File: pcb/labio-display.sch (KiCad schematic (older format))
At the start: 0 parts

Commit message: add schematics for display and dio (dpad, servo, motor, encoder)
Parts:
- added P?: CONN_01X12, symbol CONN_01X12
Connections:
- new net GND: P?.1 (P1), P?.12 (P12), P?.8 (P8)
- new net OLED_MOSI: P?.3 (P3)
- new net OLED_SCK: P?.4 (P4)
- new net VDD_3V3: P?.10 (P10), P?.11 (P11), P?.9 (P9)
- new net ~OLED_CS: P?.7 (P7)
- new net ~OLED_RST: P?.6 (P6)
- no-connect marks 0 -> 2
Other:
- note added: "CFAL12832D-B* OLED Display\n3-wire SPI mode."
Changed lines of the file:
@@
 $Descr A4 11693 8268
 encoding utf-8
-Sheet 1 7
+Sheet 5 8
 Title ""
 Date ""
@@
 Comment4 ""
 $EndDescr
+$Comp
+L CONN_01X12 P?
+U 1 1 575D4CD5
+P 5700 2950
+F 0 "P?" H 5700 3600 50  0000 C CNN
+F 1 "CONN_01X12" V 5800 2950 50  0000 C CNN
+F 2 "" H 5700 2950 50  0000 C CNN
+F 3 "" H 5700 2950 50  0000 C CNN
+	1    5700 2950
+	1    0    0    -1
+$EndComp
+Text Notes 4500 2100 0    60   ~ 0
+CFAL12832D-B* OLED Display\n3-wire SPI mode.
+$Comp
+L GND #PWR?
+U 1 1 575D4D1A
+P 4500 3600
+F 0 "#PWR?" H 4500 3350 50  0001 C CNN
+F 1 "GND" H 4500 3450 50  0000 C CNN
+F 2 "" H 4500 3600 50  0000 C CNN
+F 3 "" H 4500 3600 50  0000 C CNN
+	1    4500 3600
+	1    0    0    -1
+$EndComp
+Wire Wire Line
+	4500 2400 4500 3600
+Wire Wire Line
+	4500 3500 5500 3500
+Wire Wire Line
+	4500 2400 5500 2400
+Connection ~ 4500 3500
+Text HLabel 5000 3300 0    60   Input ~ 0
+VDD_3V3
+Wire Wire Line
+	5000 3300 5500 3300
+Wire Wire Line
+	5100 3300 5100 3400
+Wire Wire Line
+	5100 3400 5500 3400
+Connection ~ 5100 3300
+Wire Wire Line
+	5500 3200 5200 3200
+Wire Wire Line
+	5200 3200 5200 3300
+Connection ~ 5200 3300
+Wire Wire Line
+	5500 3100 4500 3100
+Connection ~ 4500 3100
+Text HLabel 5300 3000 0    60   Input ~ 0
+~OLED_CS
+Text HLabel 5300 2900 0    60   Input ~ 0
+~OLED_RST
+NoConn ~ 5500 2800
+Text HLabel 5300 2700 0    60   Input ~ 0
+OLED_SCK
+Text HLabel 5300 2600 0    60   Input ~ 0
+OLED_MOSI
+NoConn ~ 5500 2500
+Wire Wire Line
+	5300 2600 5500 2600
+Wire Wire Line
+	5300 2700 5500 2700
+Wire Wire Line
+	5300 2900 5500 2900
+Wire Wire Line
+	5300 3000 5500 3000
 $EndSCHEMATC

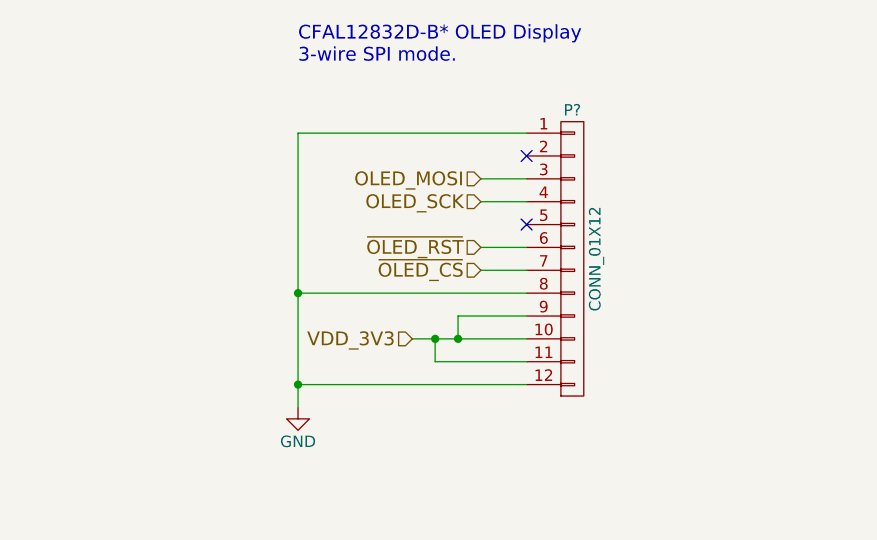
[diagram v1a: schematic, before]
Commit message: add imu sensors, make top level connections
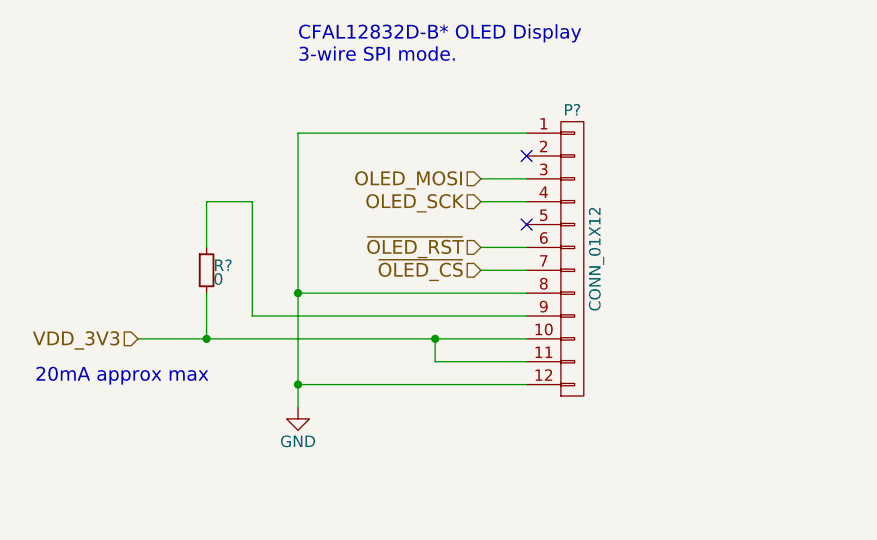
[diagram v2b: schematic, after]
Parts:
- added R?: 0, symbol R_Small
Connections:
- net VDD_3V3: now also R?.2; no longer P?.9 (P9)
- new net: P?.9 (P9), R?.1
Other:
- note added: "20mA approx max"

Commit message: finish rpi to module connections
* use dip switches to disable/configure blocks
* add light sensor
* fix motor controller sense resistors
* fix overused jtag probe pins
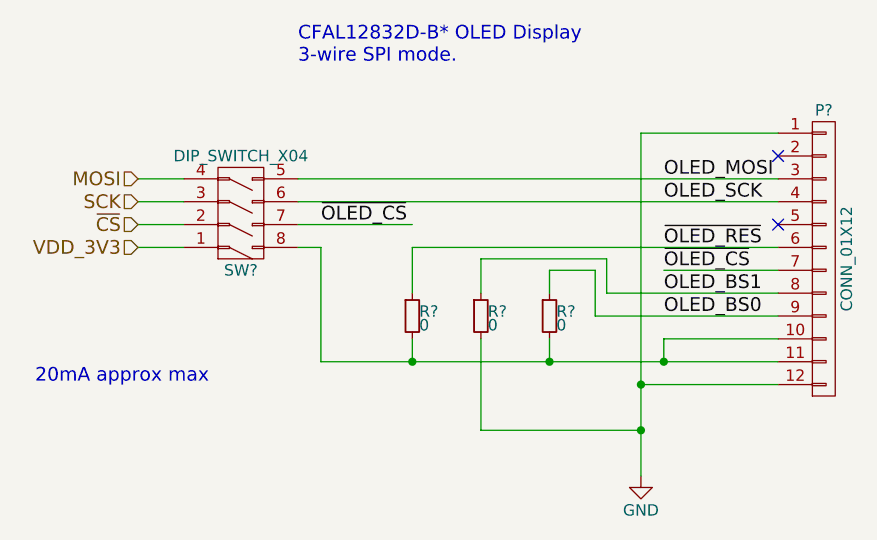
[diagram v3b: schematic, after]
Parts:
- added R? (x2): 0, symbol R_Small
- added SW?: DIP_SWITCH_X04, symbol DIP_SWITCH_X04
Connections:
- net labels added: MOSI, OLED_BS0, OLED_BS1, SCK, ~CS, ~OLED_RES
- net labels removed: ~OLED_RST
- wire segments 16 -> 35
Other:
- moved on the sheet: P?, R?
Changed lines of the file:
@@
 $Descr A4 11693 8268
 encoding utf-8
-Sheet 5 7
+Sheet 4 7
 Title ""
 Date ""
@@
 L CONN_01X12 P?
 U 1 1 575D4CD5
-P 5700 2950
-F 0 "P?" H 5700 3600 50  0000 C CNN
-F 1 "CONN_01X12" V 5800 2950 50  0000 C CNN
-F 2 "" H 5700 2950 50  0000 C CNN
-F 3 "" H 5700 2950 50  0000 C CNN
-	1    5700 2950
+P 6800 2950
+F 0 "P?" H 6800 3600 50  0000 C CNN
+F 1 "CONN_01X12" V 6900 2950 50  0000 C CNN
+F 2 "" H 6800 2950 50  0000 C CNN
+F 3 "" H 6800 2950 50  0000 C CNN
+	1    6800 2950
 	1    0    0    -1
 $EndComp
@@
 L GND #PWR?
 U 1 1 575D4D1A
-P 4500 3600
-F 0 "#PWR?" H 4500 3350 50  0001 C CNN
-F 1 "GND" H 4500 3450 50  0000 C CNN
-F 2 "" H 4500 3600 50  0000 C CNN
-F 3 "" H 4500 3600 50  0000 C CNN
-	1    4500 3600
+P 6000 3900
+F 0 "#PWR?" H 6000 3650 50  0001 C CNN
+F 1 "GND" H 6000 3750 50  0000 C CNN
+F 2 "" H 6000 3900 50  0000 C CNN
+F 3 "" H 6000 3900 50  0000 C CNN
+	1    6000 3900
 	1    0    0    -1
 $EndComp
 Wire Wire Line
-	4500 2400 4500 3600
+	6000 2400 6000 3500
 Wire Wire Line
-	4500 3500 5500 3500
+	6000 3500 6000 3700
 Wire Wire Line
-	4500 2400 5500 2400
-Connection ~ 4500 3500
-Text HLabel 3800 3300 0    60   Input ~ 0
-VDD_3V3
-Wire Wire Line
-	3800 3300 5500 3300
-Wire Wire Line
-	5100 3300 5100 3400
-Wire Wire Line
-	5100 3400 5500 3400
-Connection ~ 5100 3300
+	6000 3700 6000 3900
 Wire Wire Line
-	4300 3200 5500 3200
+	6000 3500 6600 3500
 Wire Wire Line
-	5500 3100 4500 3100
-Connection ~ 4500 3100
-Text HLabel 5300 3000 0    60   Input ~ 0
-~OLED_CS
-Text HLabel 5300 2900 0    60   Input ~ 0
-~OLED_RST
-NoConn ~ 5500 2800
-Text HLabel 5300 2700 0    60   Input ~ 0
-OLED_SCK
-Text HLabel 5300 2600 0    60   Input ~ 0
-OLED_MOSI
-NoConn ~ 5500 2500
-Wire Wire Line
-	5300 2600 5500 2600
-Wire Wire Line
-	5300 2700 5500 2700
-Wire Wire Line
-	5300 2900 5500 2900
-Wire Wire Line
-	5300 3000 5500 3000
+	6000 2400 6600 2400
+Connection ~ 6000 3500
+Text HLabel 3800 2900 0    60   Input ~ 0
+VDD_3V3
+Text HLabel 3800 2800 0    60   Input ~ 0
+~CS
+NoConn ~ 6600 2800
+Text HLabel 3800 2700 0    60   Input ~ 0
+SCK
+Text HLabel 3800 2600 0    60   Input ~ 0
+MOSI
+NoConn ~ 6600 2500
 $Bitmap
 Pos 9150 3050
@@
 03 00 00 00 00 F4 24 84 F2 00 00 00 00 00 3D 09 A1 3C 00 00 00 00 40 4F 42 28 0F 00 00 00 00 D0
 93 10 CA 03 00 00 00 00 F4 24 84 F2 00 00 00 00 00 3D 09 A1 3C 00 00 00 00 40 4F FA 3F 4E 16 A4
-A2 80 4C E9 AA 00 00 00 00 49 45 4E 44 AE 42 60 82 49
+A2 80 4C E9 AA 00 00 00 00 49 45 4E 44 AE 42 60 82 FF
 EndData
 $EndBitmap
@@
 L R_Small R?
 U 1 1 5766D812
-P 4100 3000
-F 0 "R?" H 4130 3020 50  0000 L CNN
-F 1 "0" H 4130 2960 50  0000 L CNN
-F 2 "" H 4100 3000 50  0000 C CNN
-F 3 "" H 4100 3000 50  0000 C CNN
-	1    4100 3000
+P 5000 3200
+F 0 "R?" H 5030 3220 50  0000 L CNN
+F 1 "0" H 5030 3160 50  0000 L CNN
+F 2 "" H 5000 3200 50  0000 C CNN
+F 3 "" H 5000 3200 50  0000 C CNN
+	1    5000 3200
+	1    0    0    -1
+$EndComp
+$Comp
+L DIP_SWITCH_X04 SW?
+U 1 1 576D7976
+P 4250 2750
+F 0 "SW?" H 4250 3000 50  0000 C CNN
+F 1 "DIP_SWITCH_X04" H 4250 2500 50  0000 C CNN
+F 2 "" H 4250 1550 50  0000 C CNN
+F 3 "" H 4250 1550 50  0000 C CNN
+	1    4250 2750
+	1    0    0    1
+$EndComp
+$Comp
+L R_Small R?
+U 1 1 576D79C4
+P 5600 3200
+F 0 "R?" H 5630 3220 50  0000 L CNN
+F 1 "0" H 5630 3160 50  0000 L CNN
+F 2 "" H 5600 3200 50  0000 C CNN
+F 3 "" H 5600 3200 50  0000 C CNN
+	1    5600 3200
+	1    0    0    -1
+$EndComp
+Wire Wire Line
+	3800 2900 4000 2900
+Wire Wire Line
+	4000 2600 3800 2600
+Wire Wire Line
+	3800 2700 4000 2700
+Wire Wire Line
+	4000 2800 3800 2800
+Wire Wire Line
+	4500 2600 6600 2600
+Wire Wire Line
+	6600 2700 4500 2700
+Wire Wire Line
+	4600 3400 5000 3400
+Wire Wire Line
+	5000 3400 5600 3400
+Wire Wire Line
+	5600 3400 6100 3400
+Wire Wire Line
+	6100 3400 6600 3400
+Wire Wire Line
+	4600 3400 4600 2900
+Wire Wire Line
+	4600 2900 4500 2900
+Wire Wire Line
+	6600 3300 6100 3300
+Wire Wire Line
+	6100 3300 6100 3400
+Connection ~ 6100 3400
+Wire Wire Line
+	5600 3100 5600 3000
+Wire Wire Line
+	5600 3000 5800 3000
+Wire Wire Line
+	5800 3000 5800 3200
+Wire Wire Line
+	5800 3200 6600 3200
+Wire Wire Line
+	5600 3300 5600 3400
+Connection ~ 5600 3400
+Wire Wire Line
+	5000 3300 5000 3400
+Connection ~ 5000 3400
+Wire Wire Line
+	6600 2900 5000 2900
+Wire Wire Line
+	5000 2900 5000 3100
+$Comp
+L R_Small R?
+U 1 1 576D7E44
+P 5300 3200
+F 0 "R?" H 5330 3220 50  0000 L CNN
+F 1 "0" H 5330 3160 50  0000 L CNN
+F 2 "" H 5300 3200 50  0000 C CNN
+F 3 "" H 5300 3200 50  0000 C CNN
+	1    5300 3200
 	1    0    0    -1
 $EndComp
 Wire Wire Line
-	4300 3200 4300 2700
+	5300 3300 5300 3700
+Wire Wire Line
+	5300 3700 6000 3700
+Connection ~ 6000 3700
+Wire Wire Line
+	6600 3000 6100 3000
+Text Label 6100 3000 0    60   ~ 0
+~OLED_CS
+Text Label 4600 2800 0    60   ~ 0
+~OLED_CS
+Wire Wire Line
+	4500 2800 5000 2800
+Text Label 6100 2700 0    60   ~ 0
+OLED_SCK
+Text Label 6100 2600 0    60   ~ 0
+OLED_MOSI
+Wire Wire Line
+	6600 3100 5850 3100
 Wire Wire Line
-	4300 2700 4100 2700
+	5850 3100 5850 2950
 Wire Wire Line
-	4100 2700 4100 2900
+	5850 2950 5300 2950
 Wire Wire Line
-	4100 3100 4100 3300
-Connection ~ 4100 3300
+	5300 2950 5300 3100
+Text Label 6100 3100 0    60   ~ 0
+OLED_BS1
+Text Label 6100 3200 0    60   ~ 0
+OLED_BS0
+Text Label 6100 2900 0    60   ~ 0
+~OLED_RES
 $EndSCHEMATC

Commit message: make extra footprints. start floorplan. fix display nets. add power expansion header.
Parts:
- P401: renamed from P?; footprint (none) -> labio-special:SFVxxR-xSTxxHLF
- R401, R402, R403: renamed from R?; footprint (none) -> Resistors_SMD:R_0603
- SW401: renamed from SW?; footprint (none) -> labio-special:DIP-8_W7.62mm_SMT
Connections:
- wire segments 35 -> 30
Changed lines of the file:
@@
 $Descr A4 11693 8268
 encoding utf-8
-Sheet 4 8
+Sheet 4 9
 Title ""
 Date ""
@@
 $EndDescr
 $Comp
-L CONN_01X12 P?
+L CONN_01X12 P401
 U 1 1 575D4CD5
 P 6800 2950
-F 0 "P?" H 6800 3600 50  0000 C CNN
+F 0 "P401" H 6800 3600 50  0000 C CNN
 F 1 "CONN_01X12" V 6900 2950 50  0000 C CNN
-F 2 "" H 6800 2950 50  0000 C CNN
+F 2 "labio-special:SFVxxR-xSTxxHLF" H 6800 2950 50  0001 C CNN
 F 3 "" H 6800 2950 50  0000 C CNN
 	1    6800 2950
@@
 CFAL12832D-B* OLED Display\n3-wire SPI mode.
 $Comp
-L GND #PWR?
+L GND #PWR09
 U 1 1 575D4D1A
 P 6000 3900
-F 0 "#PWR?" H 6000 3650 50  0001 C CNN
+F 0 "#PWR09" H 6000 3650 50  0001 C CNN
 F 1 "GND" H 6000 3750 50  0000 C CNN
 F 2 "" H 6000 3900 50  0000 C CNN
@@
 $EndComp
 Wire Wire Line
-	6000 2400 6000 3500
-Wire Wire Line
-	6000 3500 6000 3700
-Wire Wire Line
-	6000 3700 6000 3900
+	6000 2400 6000 3900
 Wire Wire Line
 	6000 3500 6600 3500
@@
 03 00 00 00 00 F4 24 84 F2 00 00 00 00 00 3D 09 A1 3C 00 00 00 00 40 4F 42 28 0F 00 00 00 00 D0
 93 10 CA 03 00 00 00 00 F4 24 84 F2 00 00 00 00 00 3D 09 A1 3C 00 00 00 00 40 4F FA 3F 4E 16 A4
-A2 80 4C E9 AA 00 00 00 00 49 45 4E 44 AE 42 60 82 3B
+A2 80 4C E9 AA 00 00 00 00 49 45 4E 44 AE 42 60 82 00
 EndData
 $EndBitmap
@@
 20mA approx max
 $Comp
-L R_Small R?
+L R_Small R401
 U 1 1 5766D812
 P 5000 3200
-F 0 "R?" H 5030 3220 50  0000 L CNN
+F 0 "R401" H 5030 3220 50  0000 L CNN
 F 1 "0" H 5030 3160 50  0000 L CNN
-F 2 "" H 5000 3200 50  0000 C CNN
+F 2 "Resistors_SMD:R_0603" H 5000 3200 50  0001 C CNN
 F 3 "" H 5000 3200 50  0000 C CNN
 	1    5000 3200
@@
 $EndComp
 $Comp
-L DIP_SWITCH_X04 SW?
+L DIP_SWITCH_X04 SW401
 U 1 1 576D7976
 P 4250 2750
-F 0 "SW?" H 4250 3000 50  0000 C CNN
+F 0 "SW401" H 4250 3000 50  0000 C CNN
 F 1 "DIP_SWITCH_X04" H 4250 2500 50  0000 C CNN
-F 2 "" H 4250 1550 50  0000 C CNN
+F 2 "labio-special:DIP-8_W7.62mm_SMT" H 4250 1550 50  0001 C CNN
 F 3 "" H 4250 1550 50  0000 C CNN
 	1    4250 2750
@@
 $EndComp
 $Comp
-L R_Small R?
+L R_Small R403
 U 1 1 576D79C4
 P 5600 3200
-F 0 "R?" H 5630 3220 50  0000 L CNN
+F 0 "R403" H 5630 3220 50  0000 L CNN
 F 1 "0" H 5630 3160 50  0000 L CNN
-F 2 "" H 5600 3200 50  0000 C CNN
+F 2 "Resistors_SMD:R_0603" H 5600 3200 50  0001 C CNN
 F 3 "" H 5600 3200 50  0000 C CNN
 	1    5600 3200
@@
 	6600 2700 4500 2700
 Wire Wire Line
-	4600 3400 5000 3400
-Wire Wire Line
-	5000 3400 5600 3400
-Wire Wire Line
-	5600 3400 6100 3400
-Wire Wire Line
-	6100 3400 6600 3400
+	4600 3400 6600 3400
 Wire Wire Line
 	4600 3400 4600 2900
@@
 	5000 2900 5000 3100
 $Comp
-L R_Small R?
+L R_Small R402
 U 1 1 576D7E44
 P 5300 3200
-F 0 "R?" H 5330 3220 50  0000 L CNN
+F 0 "R402" H 5330 3220 50  0000 L CNN
 F 1 "0" H 5330 3160 50  0000 L CNN
-F 2 "" H 5300 3200 50  0000 C CNN
+F 2 "Resistors_SMD:R_0603" H 5300 3200 50  0001 C CNN
 F 3 "" H 5300 3200 50  0000 C CNN
 	1    5300 3200
